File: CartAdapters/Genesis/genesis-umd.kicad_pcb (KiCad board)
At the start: 2 copper layers, 26.7 x 94.6 mm, 4 parts, among them CON101 UMDv2-CONN, CON102 GENESIS-CONN, U101 MCP23008T-E_SS

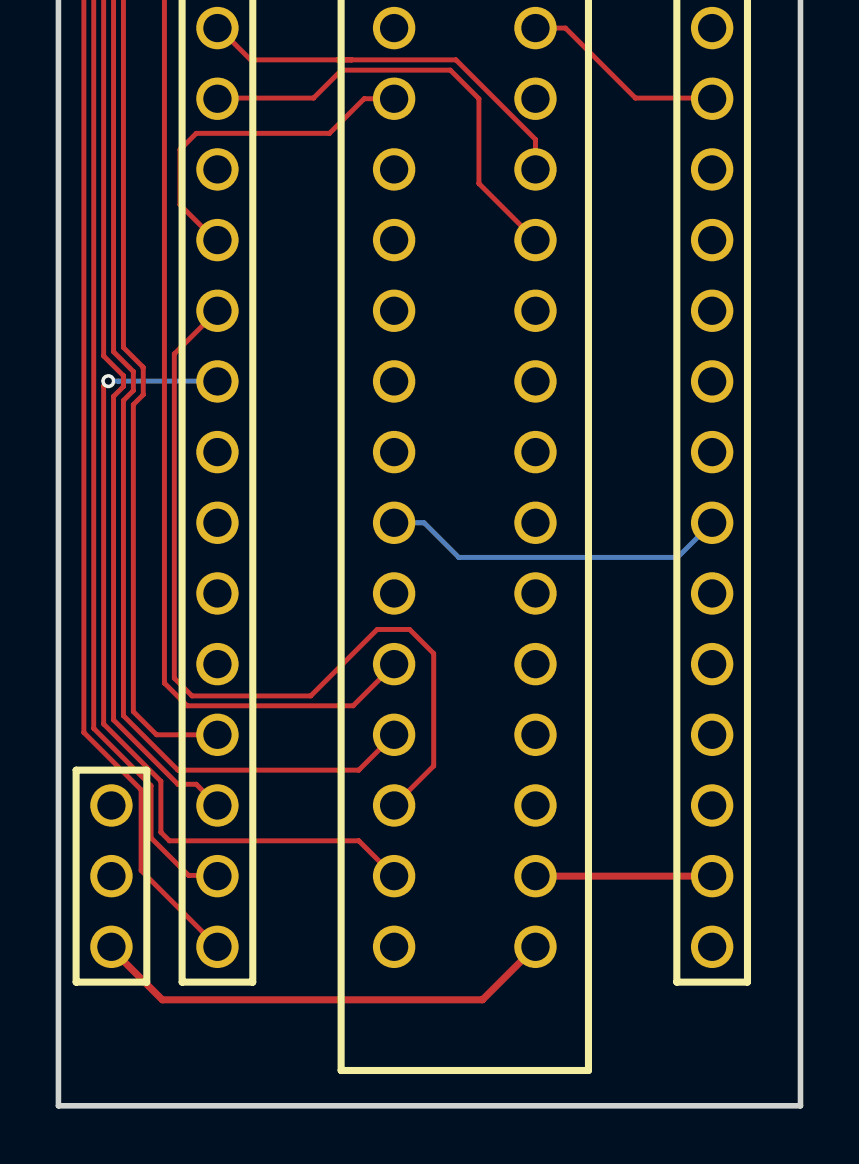
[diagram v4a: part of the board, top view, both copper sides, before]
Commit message: proper nCART wiring for Genesis adapter
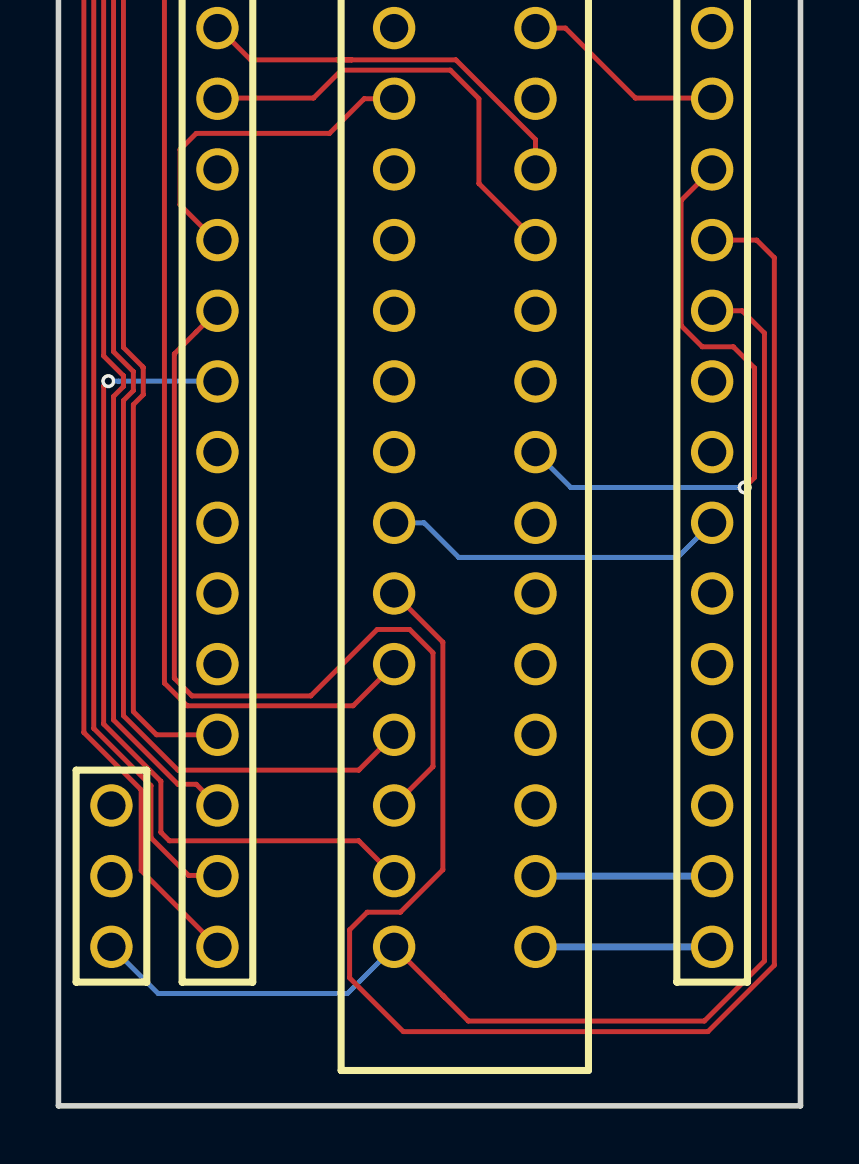
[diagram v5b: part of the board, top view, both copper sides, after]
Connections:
- CON101 pad 42: /~CART~ -> Net-(CON101-Pad42)
- CON101 pad 67: GND -> /~CART~
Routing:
- net /~VRES~: track 0.00 -> 61.6 mm
- net /~CART~: track 0.00 -> 51.7 mm
- net /D5: track 0.00 -> 21.8 mm, vias 0 -> 1
- net GND: track 33.8 -> 23.3 mm
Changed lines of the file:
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@@
     (thickness 1.6)
     (drawings 4)
-    (tracks 245)
+    (tracks 277)
     (zones 0)
     (modules 4)
-    (nets 76)
+    (nets 77)
   )
   (page A4)
@@
   (net 74 "Net-(CON101-Pad65)")
   (net 75 /~M3~)
+  (net 76 "Net-(CON101-Pad42)")
   (net_class Default "This is the default net class."
     (clearance 0.1778)
@@
     (add_net "Net-(CON101-Pad4)")
     (add_net "Net-(CON101-Pad40)")
+    (add_net "Net-(CON101-Pad42)")
     (add_net "Net-(CON101-Pad5)")
     (add_net "Net-(CON101-Pad60)")
@@
     (fp_line (start 16.51 1.27) (end 19.05 1.27) (layer F.SilkS) (width 0.254))
     (pad 67 thru_hole circle (at -3.81 78.74 270) (size 1.524 1.524) (drill 1.016) (layers *.Cu *.Mask)
-      (net 2 GND))
+      (net 38 /~CART~))
     (pad 66 thru_hole circle (at -3.81 76.2 270) (size 1.524 1.524) (drill 1.016) (layers *.Cu *.Mask)
       (net 73 "Net-(CON101-Pad66)"))
@@
       (net 39 /~VRES~))
     (pad 42 thru_hole circle (at 17.78 55.88) (size 1.524 1.524) (drill 1.016) (layers *.Cu *.Mask)
-      (net 38 /~CART~))
+      (net 76 "Net-(CON101-Pad42)"))
     (pad 41 thru_hole circle (at 17.78 58.42) (size 1.524 1.524) (drill 1.016) (layers *.Cu *.Mask)
       (net 37 /A6))
@@
   (segment (start 153.67 66.04) (end 152.59237 66.04) (width 0.254) (layer F.Cu) (net 2))
   (segment (start 152.59237 66.04) (end 147.3454 66.04) (width 0.254) (layer F.Cu) (net 2))
-  (segment (start 147.32 144.78) (end 145.415 146.685) (width 0.254) (layer F.Cu) (net 2))
-  (segment (start 145.415 146.685) (end 133.9088 146.685) (width 0.254) (layer F.Cu) (net 2))
-  (segment (start 133.9088 146.685) (end 132.0292 144.8054) (width 0.254) (layer F.Cu) (net 2))
   (via (at 146.7104 59.817) (size 0.508) (drill 0.254) (layers F.Cu B.Cu) (net 2))
   (segment (start 147.32 66.04) (end 147.32 60.4266) (width 0.254) (layer F.Cu) (net 2))
@@
   (segment (start 144.9498 60.9092) (end 146.6342 60.9092) (width 0.254) (layer B.Cu) (net 2))
   (segment (start 146.6342 60.9092) (end 146.6596 60.8838) (width 0.254) (layer B.Cu) (net 2))
+  (segment (start 147.32 144.78) (end 153.67 144.78) (width 0.254) (layer B.Cu) (net 2))
   (segment (start 133.0706 68.3006) (end 133.0706 63.4746) (width 0.1778) (layer B.Cu) (net 3))
   (segment (start 135.89 71.12) (end 133.0706 68.3006) (width 0.1778) (layer B.Cu) (net 3))
@@
   (segment (start 133.146776 139.136085) (end 131.089367 137.078676) (width 0.1778) (layer F.Cu) (net 29))
   (segment (start 147.32 68.58) (end 153.6954 68.58) (width 0.254) (layer F.Cu) (net 30))
-  (segment (start 147.32 142.24) (end 153.5938 142.24) (width 0.254) (layer F.Cu) (net 30))
+  (segment (start 147.32 142.24) (end 153.67 142.24) (width 0.254) (layer B.Cu) (net 30))
+  (segment (start 154.74763 121.92) (end 155.5496 122.72197) (width 0.1778) (layer F.Cu) (net 38))
+  (segment (start 153.67 121.92) (end 154.74763 121.92) (width 0.1778) (layer F.Cu) (net 38))
+  (segment (start 155.5496 122.72197) (end 155.5496 145.288) (width 0.1778) (layer F.Cu) (net 38))
+  (segment (start 155.5496 145.288) (end 153.3906 147.447) (width 0.1778) (layer F.Cu) (net 38))
+  (segment (start 153.3906 147.447) (end 144.907 147.447) (width 0.1778) (layer F.Cu) (net 38))
+  (segment (start 144.907 147.447) (end 143.9926 146.5326) (width 0.1778) (layer F.Cu) (net 38))
+  (segment (start 144.0688 146.6088) (end 143.9926 146.5326) (width 0.1778) (layer F.Cu) (net 38))
+  (segment (start 143.9926 146.5326) (end 142.24 144.78) (width 0.1778) (layer F.Cu) (net 38))
+  (segment (start 142.24 144.78) (end 140.5636 146.4564) (width 0.1778) (layer B.Cu) (net 38))
+  (segment (start 133.7564 146.4564) (end 132.08 144.78) (width 0.1778) (layer B.Cu) (net 38))
+  (segment (start 140.5636 146.4564) (end 133.7564 146.4564) (width 0.1778) (layer B.Cu) (net 38))
+  (segment (start 143.9926 142.009878) (end 143.9926 133.8326) (width 0.1778) (layer F.Cu) (net 39))
+  (segment (start 142.467078 143.5354) (end 143.9926 142.009878) (width 0.1778) (layer F.Cu) (net 39))
+  (segment (start 140.6398 144.1704) (end 141.2748 143.5354) (width 0.1778) (layer F.Cu) (net 39))
+  (segment (start 140.6398 145.8976) (end 140.6398 144.1704) (width 0.1778) (layer F.Cu) (net 39))
+  (segment (start 153.5176 147.828) (end 142.5702 147.828) (width 0.1778) (layer F.Cu) (net 39))
+  (segment (start 142.5702 147.828) (end 140.6398 145.8976) (width 0.1778) (layer F.Cu) (net 39))
+  (segment (start 155.2702 119.38) (end 155.9052 120.015) (width 0.1778) (layer F.Cu) (net 39))
+  (segment (start 153.67 119.38) (end 155.2702 119.38) (width 0.1778) (layer F.Cu) (net 39))
+  (segment (start 155.9052 120.015) (end 155.9052 145.4404) (width 0.1778) (layer F.Cu) (net 39))
+  (segment (start 141.2748 143.5354) (end 142.467078 143.5354) (width 0.1778) (layer F.Cu) (net 39))
+  (segment (start 155.9052 145.4404) (end 153.5176 147.828) (width 0.1778) (layer F.Cu) (net 39))
+  (segment (start 143.9926 133.8326) (end 142.24 132.08) (width 0.1778) (layer F.Cu) (net 39))
+  (via (at 154.8384 128.27) (size 0.508) (drill 0.254) (layers F.Cu B.Cu) (net 40))
+  (segment (start 147.32 127) (end 148.59 128.27) (width 0.1778) (layer B.Cu) (net 40))
+  (segment (start 148.59 128.27) (end 154.8384 128.27) (width 0.1778) (layer B.Cu) (net 40))
+  (segment (start 155.194 127.9144) (end 155.194 123.9774) (width 0.1778) (layer F.Cu) (net 40))
+  (segment (start 154.8384 128.27) (end 155.194 127.9144) (width 0.1778) (layer F.Cu) (net 40))
+  (segment (start 152.5524 117.9576) (end 153.67 116.84) (width 0.1778) (layer F.Cu) (net 40))
+  (segment (start 152.5524 122.4534) (end 152.5524 117.9576) (width 0.1778) (layer F.Cu) (net 40))
+  (segment (start 155.194 123.9774) (end 154.432 123.2154) (width 0.1778) (layer F.Cu) (net 40))
+  (segment (start 154.432 123.2154) (end 153.3144 123.2154) (width 0.1778) (layer F.Cu) (net 40))
+  (segment (start 153.3144 123.2154) (end 152.5524 122.4534) (width 0.1778) (layer F.Cu) (net 40))
   (segment (start 148.39763 111.76) (end 150.91223 114.2746) (width 0.1778) (layer F.Cu) (net 41))
   (segment (start 147.32 111.76) (end 148.39763 111.76) (width 0.1778) (layer F.Cu) (net 41))
@@
   (segment (start 152.4254 130.7846) (end 153.67 129.54) (width 0.1778) (layer B.Cu) (net 69))
   (segment (start 144.56223 130.7846) (end 152.4254 130.7846) (width 0.1778) (layer B.Cu) (net 69))
-  (segment (start 142.24 139.7) (end 143.6624 138.2776) (width 0.1778) (layer F.Cu) (net 75))
-  (segment (start 143.6624 138.2776) (end 143.6624 134.239) (width 0.1778) (layer F.Cu) (net 75))
-  (segment (start 143.6624 134.239) (end 142.7988 133.3754) (width 0.1778) (layer F.Cu) (net 75))
+  (segment (start 143.636989 138.303011) (end 143.636989 134.213589) (width 0.1778) (layer F.Cu) (net 75))
+  (segment (start 142.24 139.7) (end 143.636989 138.303011) (width 0.1778) (layer F.Cu) (net 75))
+  (segment (start 143.636989 134.213589) (end 142.7988 133.3754) (width 0.1778) (layer F.Cu) (net 75))
   (segment (start 142.7988 133.3754) (end 141.6304 133.3754) (width 0.1778) (layer F.Cu) (net 75))
+  (segment (start 134.3406 123.4694) (end 135.128001 122.681999) (width 0.1778) (layer F.Cu) (net 75))
+  (segment (start 135.128001 122.681999) (end 135.89 121.92) (width 0.1778) (layer F.Cu) (net 75))
+  (segment (start 139.2428 135.763) (end 134.9756 135.763) (width 0.1778) (layer F.Cu) (net 75))
+  (segment (start 134.3406 135.128) (end 134.3406 123.4694) (width 0.1778) (layer F.Cu) (net 75))
+  (segment (start 134.9756 135.763) (end 134.3406 135.128) (width 0.1778) (layer F.Cu) (net 75))
   (segment (start 141.6304 133.3754) (end 139.2428 135.763) (width 0.1778) (layer F.Cu) (net 75))
-  (segment (start 139.2428 135.763) (end 134.9756 135.763) (width 0.1778) (layer F.Cu) (net 75))
-  (segment (start 134.9756 135.763) (end 134.3406 135.128) (width 0.1778) (layer F.Cu) (net 75))
-  (segment (start 134.3406 123.4694) (end 135.89 121.92) (width 0.1778) (layer F.Cu) (net 75))
-  (segment (start 134.3406 135.128) (end 134.3406 123.4694) (width 0.1778) (layer F.Cu) (net 75))
   (zone (net 0) (net_name "") (layers F&B.Cu) (hatch edge 0.508)
     (connect_pads (clearance 0.508))

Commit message: prelim routing complete on genesis adapter
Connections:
- CON101 pad 33: GND -> /GND_1
- CON101 pad 34: +5V -> /5V_1
- CON101 pad 63: +5V -> /5V_0
- CON102 pad A18: GND -> Net-(CON102-PadA18)
- CON102 pad A2: +5V -> /5V_0
- CON102 pad A31: +5V -> /5V_1
- CON102 pad A32: GND -> /GND_1
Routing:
- net /A21: track 0.00 -> 64.3 mm
- net /A5: track 0.00 -> 59.1 mm, vias 0 -> 2
- net /A6: track 0.00 -> 45.8 mm
- net /A3: track 0.00 -> 45.6 mm, vias 0 -> 1
- net /~AS~: track 0.00 -> 44.7 mm
- net /D3: track 0.00 -> 44.7 mm, vias 0 -> 1
- net /A4: track 0.00 -> 43.3 mm
- net /A2: track 0.00 -> 37.5 mm
- net /~CE~: track 0.00 -> 36.8 mm, vias 0 -> 1
- net /A1: track 0.00 -> 36.2 mm, vias 0 -> 1
- net /D11: track 0.00 -> 35.5 mm, vias 0 -> 1
- net /D2: track 0.00 -> 34.8 mm, vias 0 -> 2
- net /D13: track 0.00 -> 34.1 mm, vias 0 -> 2
- net /D10: track 0.00 -> 32.6 mm, vias 0 -> 2
- net /D1: track 0.00 -> 30.6 mm, vias 0 -> 1
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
